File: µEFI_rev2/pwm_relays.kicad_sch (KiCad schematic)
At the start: 2 parts, among them U20 TPL7407LAPWR, U22 TPL7407LAPWR

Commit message: uEFI v2 beta release
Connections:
- net CONN_18 renamed E3
- net CONN_39 renamed B4
- net CONN_40 renamed C4
- net CONN_58 renamed D3
- net CONN_63 renamed F3
- net CONN_64 renamed D4
- net CONN_65 renamed G3
- net CONN_66 renamed H3

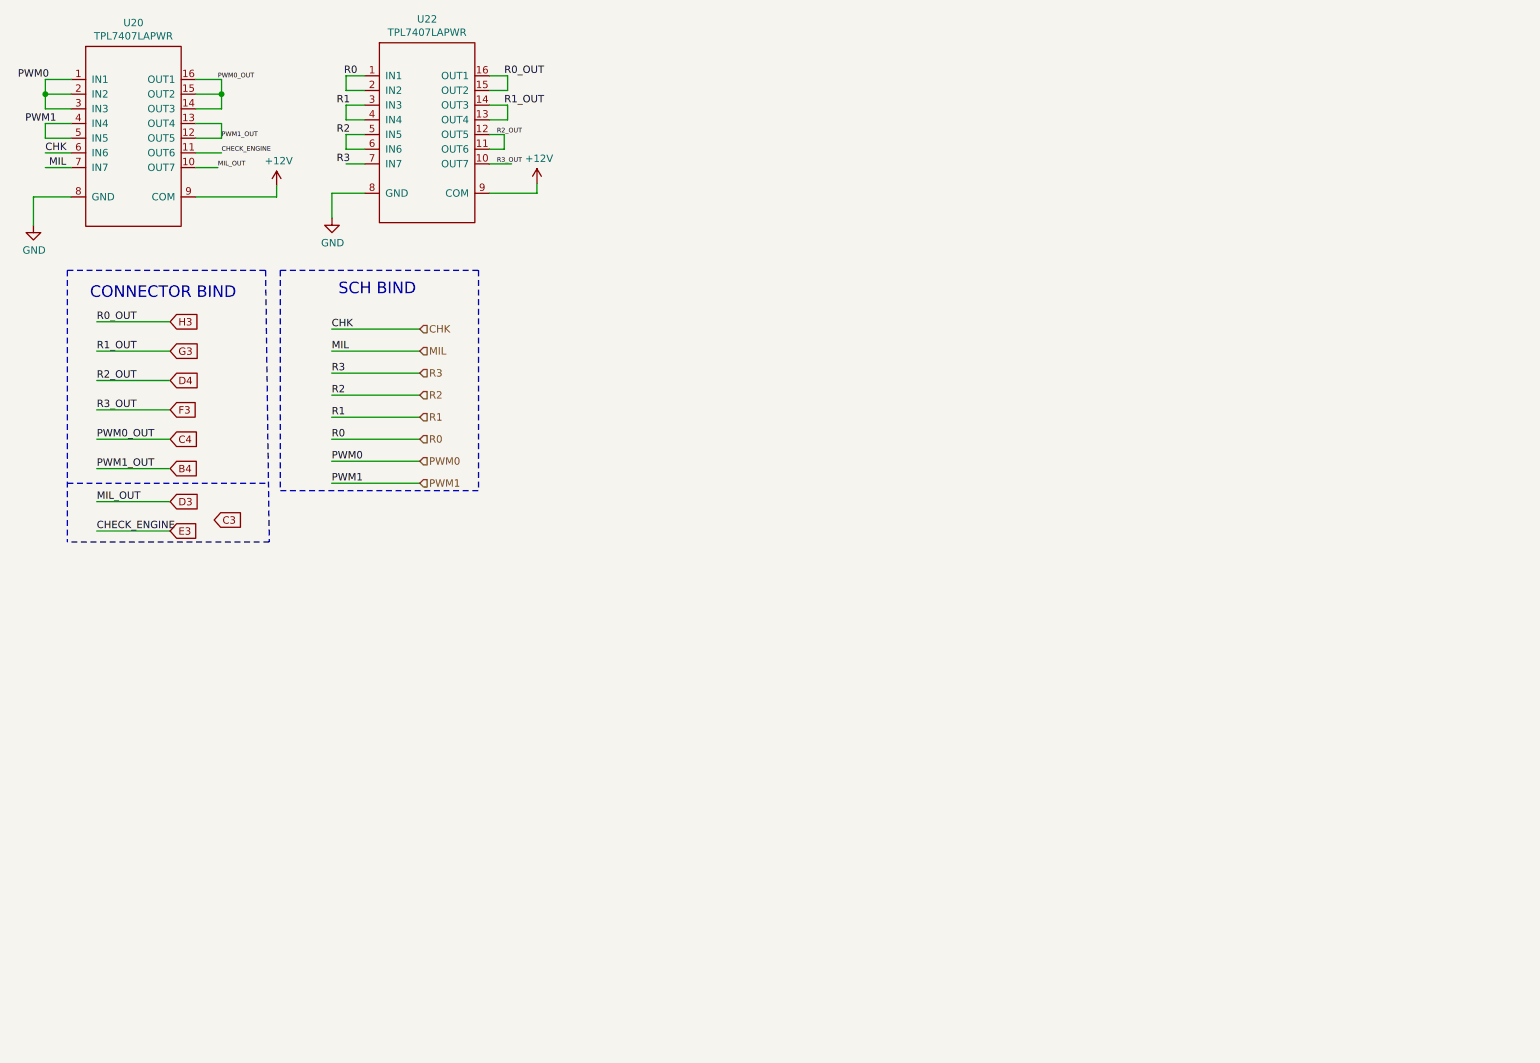
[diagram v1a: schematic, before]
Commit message: bump to kicad 6, init uEFI v3
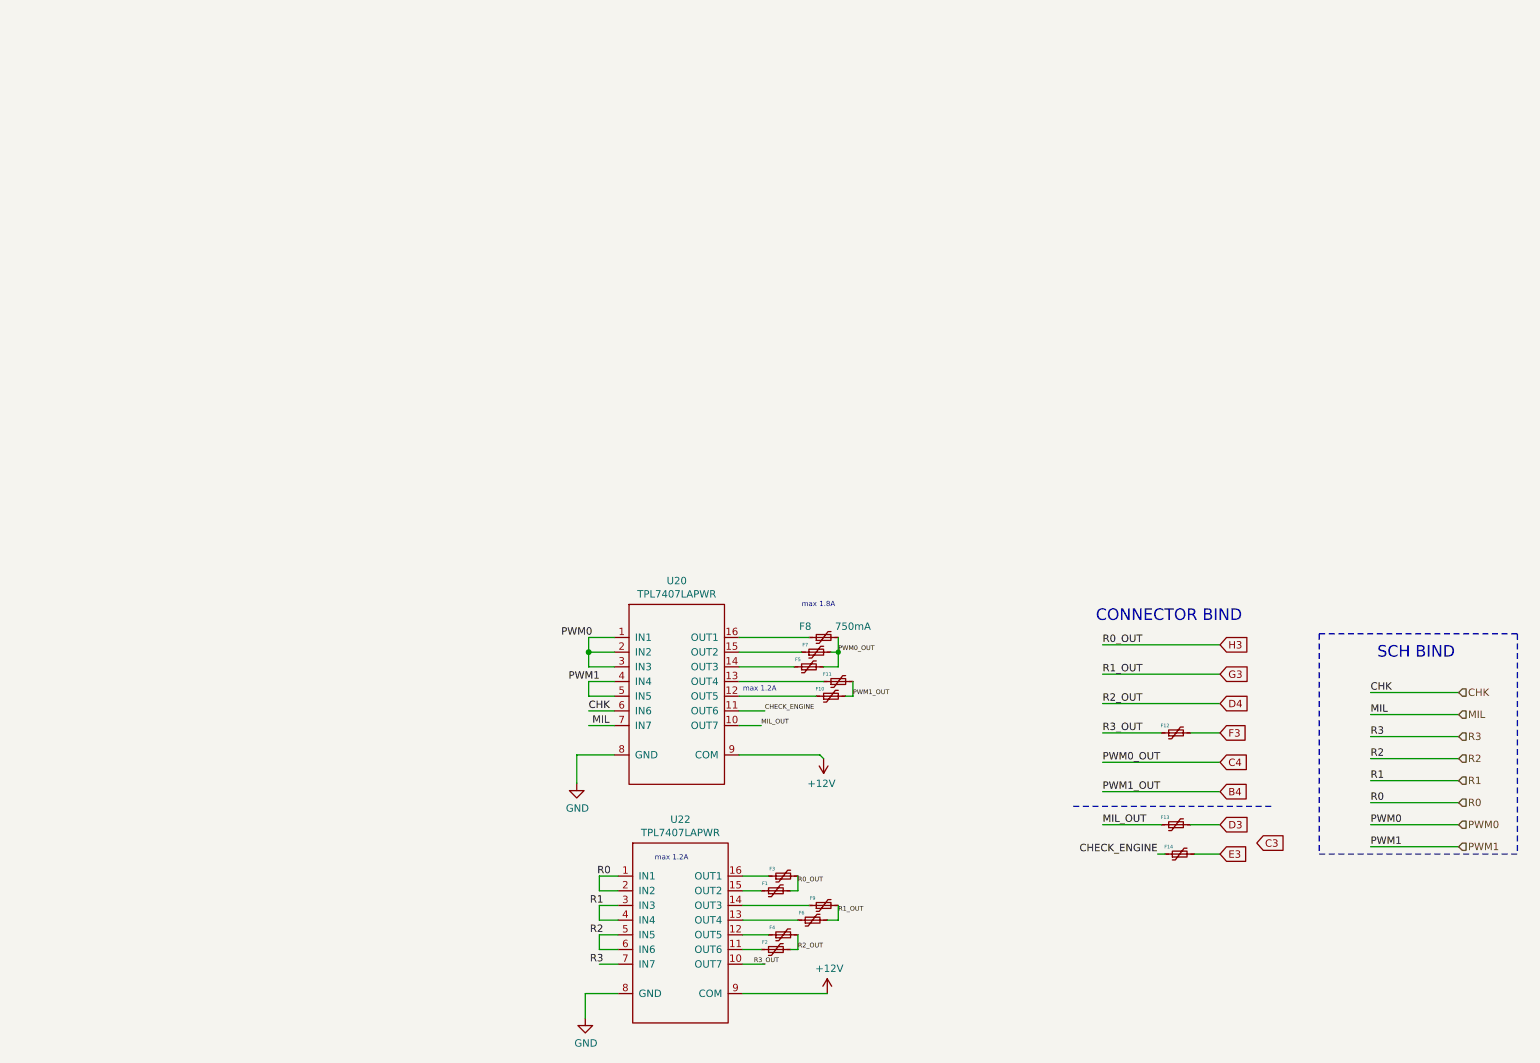
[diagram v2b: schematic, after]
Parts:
- added F1, F10, F11, F12, F13, F14, F2, F3, F4, F5, F6, F7, F8, F9: 750mA, Fuse:Fuse_0805_2012Metric, symbol Device:Polyfuse_Small
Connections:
- net B4: now also F10.2, F11.2; no longer U20.12 (OUT5), U20.13 (OUT4)
- net C4: now also F5.2, F7.2, F8.2; no longer U20.14 (OUT3), U20.15 (OUT2), U20.16 (OUT1)
- net D3: now also F13.2; no longer U20.10 (OUT7)
- net D4: now also F2.2, F4.2; no longer U22.11 (OUT6), U22.12 (OUT5)
- net E3: now also F14.2; no longer U20.11 (OUT6)
- net F3: now also F12.2; no longer U22.10 (OUT7)
- net G3: now also F6.2, F9.2; no longer U22.13 (OUT4), U22.14 (OUT3)
- net H3: now also F1.2, F3.2; no longer U22.15 (OUT2), U22.16 (OUT1)
- new net: F1.1, U22.15 (OUT2)
- new net: F7.1, U20.15 (OUT2)
- new net: F6.1, U22.13 (OUT4)
- new net: F9.1, U22.14 (OUT3)
- new net: F4.1, U22.12 (OUT5)
- new net: F11.1, U20.13 (OUT4)
- new net: F8.1, U20.16 (OUT1)
- new net: F2.1, U22.11 (OUT6)
- new net: F5.1, U20.14 (OUT3)
- new net: F10.1, U20.12 (OUT5)
- new net: F3.1, U22.16 (OUT1)
- new net CHECK_ENGINE: F14.1, U20.11 (OUT6)
- new net MIL_OUT: F13.1, U20.10 (OUT7)
- new net R3_OUT: F12.1, U22.10 (OUT7)
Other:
- note added: "max 1.2A"
- note added: "max 1.8A"
- company: (none) -> Churrosoft
- title: (none) -> uEFI
- moved on the sheet: U20, U22

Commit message: move old boards to __old
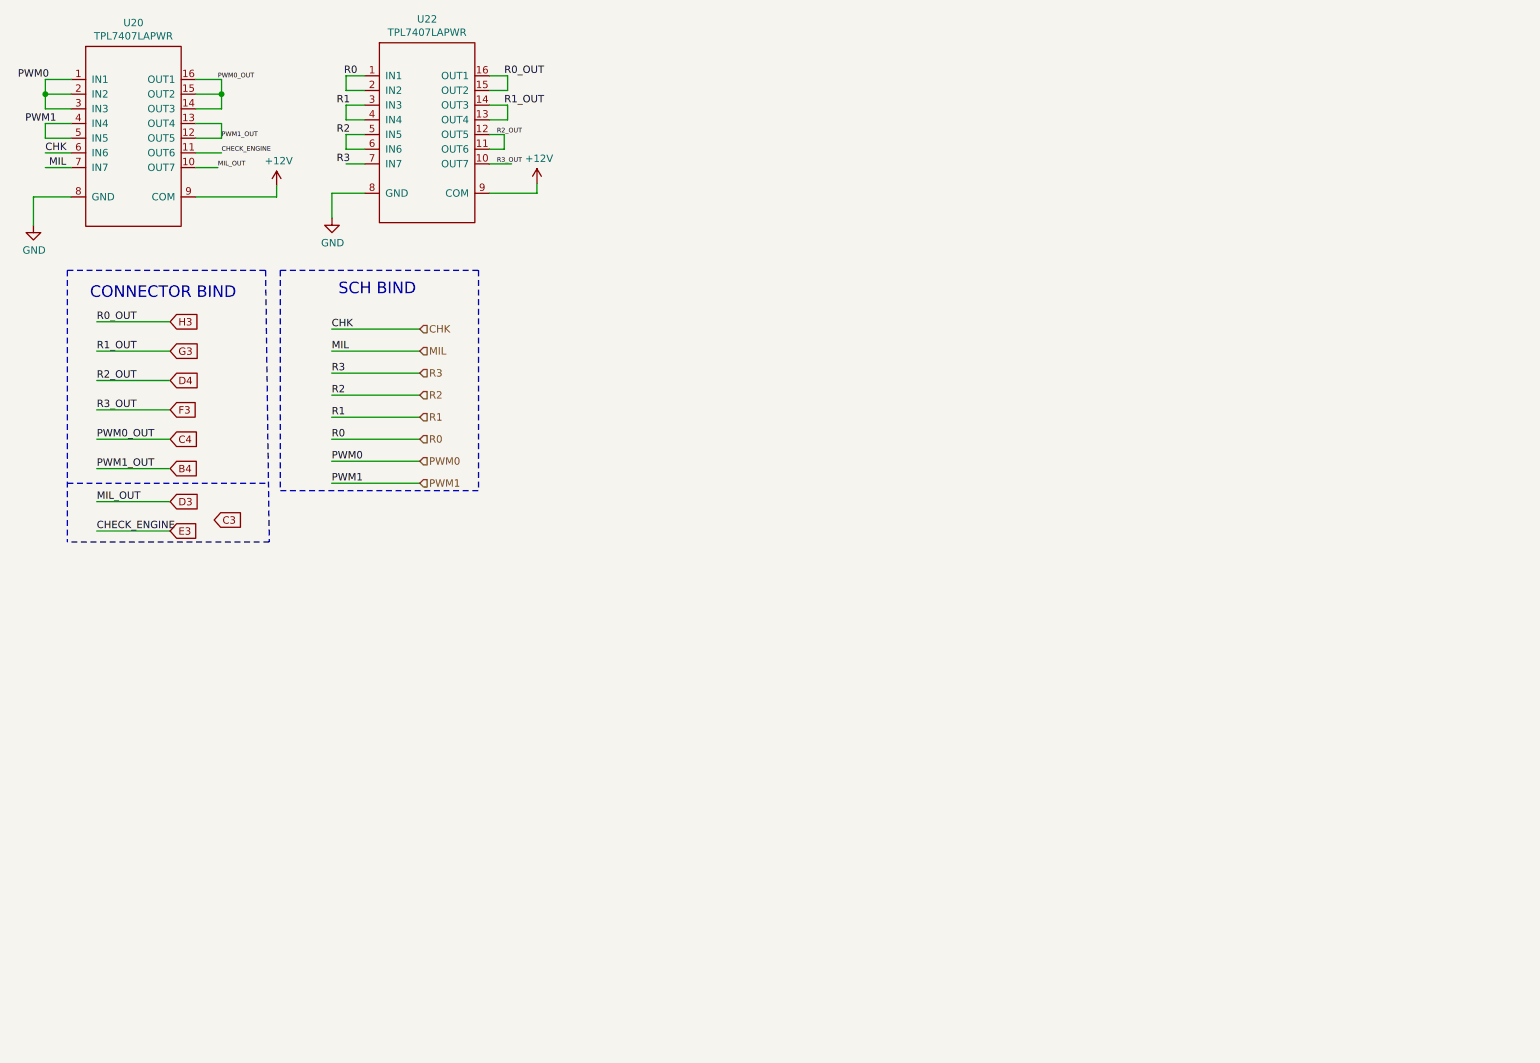
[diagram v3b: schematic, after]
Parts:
- removed F1, F10, F11, F12, F13, F14, F2, F3, F4, F5, F6, F7, F8, F9: 750mA, Fuse:Fuse_0805_2012Metric, symbol Device:Polyfuse_Small
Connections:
- net CHECK_ENGINE is gone; now on net E3: U20.11 (OUT6)
- net MIL_OUT is gone; now on net D3: U20.10 (OUT7)
- net R3_OUT is gone; now on net F3: U22.10 (OUT7)
- net B4: now also U20.12 (OUT5), U20.13 (OUT4)
- net C4: now also U20.14 (OUT3), U20.15 (OUT2), U20.16 (OUT1)
- net D4: now also U22.11 (OUT6), U22.12 (OUT5)
- net G3: now also U22.13 (OUT4), U22.14 (OUT3)
- net H3: now also U22.15 (OUT2), U22.16 (OUT1)
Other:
- note removed: "max 1.2A"
- note removed: "max 1.8A"
- company: Churrosoft -> (none)
- title: uEFI -> (none)
- moved on the sheet: U20, U22
